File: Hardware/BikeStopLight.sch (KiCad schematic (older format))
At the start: 60 parts, among them J1 ST-Link, J2 PWR, J3 BAT, J4 Conn_01x01, J5 Conn_01x01, J6 Conn_01x08, Q1 NTD4909N, U1 MCP1703A-3302_SOT23, U2 STM32L052K8Tx, U3 RFM95W-868S2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

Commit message: WIP - Started layout
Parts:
- added C25, C27: 100 nF, Capacitor_SMD:C_0805_2012Metric, symbol Device:C_Small
- added C26: TBC, Capacitor_SMD:C_0805_2012Metric, symbol Device:C_Small
- C1, C10, C11, C12, C13, C14, C15, C16, C17, C18, C19, C20, C21, C22, C23, C24, C3, C4, C5, C6, C7, C8, C9: footprint Capacitor_SMD:C_0603_1608Metric_Pad1.05x0.95mm_HandSolder -> Capacitor_SMD:C_0805_2012Metric
- C2: footprint Capacitor_SMD:C_0805_2012Metric_Pad1.15x1.40mm_HandSolder -> Capacitor_SMD:C_0805_2012Metric
- J1: footprint (none) -> Connector_PinHeader_2.54mm:PinHeader_1x04_P2.54mm_Vertical
- J2: footprint (none) -> Connector_PinHeader_2.54mm:PinHeader_1x03_P2.54mm_Vertical
- J3: footprint (none) -> Connector_PinHeader_2.54mm:PinHeader_1x02_P2.54mm_Vertical
- J4, J5: footprint (none) -> Connector_PinHeader_2.54mm:PinHeader_1x01_P2.54mm_Vertical
- J6: footprint (none) -> Connector_PinHeader_2.54mm:PinHeader_1x08_P2.54mm_Vertical
- R1, R3, R4, R5, R7: footprint Resistor_SMD:R_0603_1608Metric_Pad1.05x0.95mm_HandSolder -> Resistor_SMD:R_0805_2012Metric
- R6: value 0 Ohm -> 10 kOhm; footprint Resistor_SMD:R_0603_1608Metric_Pad1.05x0.95mm_HandSolder -> Resistor_SMD:R_0805_2012Metric
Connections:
- net labels added: BNO_INT_EXTI5, I2C1_SCL, I2C1_SDA, PWR_ON, SX_ANT, SX_DIO0, SX_DIO1, TSC_G2_IO1_S, TSC_G2_IO2, TSC_G2_IO3
- net labels removed: -BATT, INT, LED_ON, SCL, SDA
- wire segments 150 -> 182
- no-connect marks 7 -> 11
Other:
- note removed: "USB_DM"
- note removed: "USB_DP"
- moved on the sheet: J5

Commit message: WIP - Routed
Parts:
- removed J3: BAT, Connector_PinHeader_2.54mm:PinHeader_1x02_P2.54mm_Vertical, symbol Connector_Generic:Conn_01x02
- added R8: 0 Ohm, Resistor_SMD:R_0805_2012Metric, symbol Device:R_Small
- added S2: Touch_IO2, symbol Connector_Generic:Conn_01x01
- added S3: Touch_IO3, symbol Connector_Generic:Conn_01x01
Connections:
- wire segments 182 -> 183
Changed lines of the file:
@@
 Wire Wire Line
 	1100 2250 1350 2250
-$Comp
-L Connector_Generic:Conn_01x02 J3
-U 1 1 5CD40FA1
-P 8550 2900
-F 0 "J3" H 8470 2575 50  0000 C CNN
-F 1 "BAT" H 8470 2666 50  0000 C CNN
-F 2 "Connector_PinHeader_2.54mm:PinHeader_1x02_P2.54mm_Vertical" H 8550 2900 50  0001 C CNN
-F 3 "~" H 8550 2900 50  0001 C CNN
-	1    8550 2900
-	-1   0    0    1
-$EndComp
-Wire Wire Line
-	8750 2900 9450 2900
-Wire Wire Line
-	9450 2800 8750 2800
-$Comp
-L power:+BATT #PWR0108
-U 1 1 5CD4BED2
-P 9450 2800
-F 0 "#PWR0108" H 9450 2650 50  0001 C CNN
-F 1 "+BATT" H 9465 2973 50  0000 C CNN
-F 2 "" H 9450 2800 50  0001 C CNN
-F 3 "" H 9450 2800 50  0001 C CNN
-	1    9450 2800
-	1    0    0    -1
-$EndComp
 Wire Wire Line
 	950  7400 1050 7400
@@
 	1    0    0    -1
 $EndComp
-Entry Wire Line
-	3950 6150 4050 6250
 Wire Wire Line
 	7050 3500 7150 3500
@@
 F 3 "http://www.hoperf.com/upload/rf/RFM95_96_97_98W.pdf" H 3300 6900 50  0001 C CNN
 	1    6600 5250
-	1    0    0    -1
-$EndComp
-$Comp
-L power:VCC #PWR0118
-U 1 1 5CD44CB6
-P 6600 4400
-F 0 "#PWR0118" H 6600 4250 50  0001 C CNN
-F 1 "VCC" H 6617 4573 50  0000 C CNN
-F 2 "" H 6600 4400 50  0001 C CNN
-F 3 "" H 6600 4400 50  0001 C CNN
-	1    6600 4400
 	1    0    0    -1
 $EndComp
@@
 	5500 1850 6050 1850
 Wire Wire Line
-	6050 1950 5500 1950
-Wire Wire Line
 	5500 2350 6050 2350
 Wire Wire Line
@@
 	2700 1900 2700 1850
 $Comp
-L power:GND #PWR0107
-U 1 1 5CE8B7EE
-P 9450 2900
-F 0 "#PWR0107" H 9450 2650 50  0001 C CNN
-F 1 "GND" H 9455 2727 50  0000 C CNN
-F 2 "" H 9450 2900 50  0001 C CNN
-F 3 "" H 9450 2900 50  0001 C CNN
-	1    9450 2900
-	1    0    0    -1
-$EndComp
+L power:+3.3V #PWR0118
+U 1 1 5CE124DA
+P 6600 4400
+F 0 "#PWR0118" H 6600 4250 50  0001 C CNN
+F 1 "+3.3V" H 6615 4573 50  0000 C CNN
+F 2 "" H 6600 4400 50  0001 C CNN
+F 3 "" H 6600 4400 50  0001 C CNN
+	1    6600 4400
+	1    0    0    -1
+$EndComp
+$Comp
+L Device:R_Small R8
+U 1 1 5CE13172
+P 750 1550
+F 0 "R8" H 809 1596 50  0000 L CNN
+F 1 "0 Ohm" H 809 1505 50  0000 L CNN
+F 2 "Resistor_SMD:R_0805_2012Metric" H 750 1550 50  0001 C CNN
+F 3 "~" H 750 1550 50  0001 C CNN
+	1    750  1550
+	1    0    0    -1
+$EndComp
+Wire Wire Line
+	750  1450 750  1100
+Connection ~ 750  1100
+Wire Wire Line
+	750  1650 750  1950
+Wire Wire Line
+	750  1950 850  1950
+Connection ~ 850  1950
+$Comp
+L Connector_Generic:Conn_01x01 S2
+U 1 1 5CE3D1CA
+P 6250 1850
+F 0 "S2" H 6330 1892 50  0000 L CNN
+F 1 "Touch_IO2" H 6330 1801 50  0000 L CNN
+F 2 "" H 6250 1850 50  0001 C CNN
+F 3 "~" H 6250 1850 50  0001 C CNN
+	1    6250 1850
+	1    0    0    -1
+$EndComp
+$Comp
+L Connector_Generic:Conn_01x01 S3
+U 1 1 5CE3D3C0
+P 6100 1950
+F 0 "S3" H 6180 1992 50  0000 L CNN
+F 1 "Touch_IO3" H 6180 1901 50  0000 L CNN
+F 2 "" H 6100 1950 50  0001 C CNN
+F 3 "~" H 6100 1950 50  0001 C CNN
+	1    6100 1950
+	1    0    0    -1
+$EndComp
+Wire Wire Line
+	5500 1950 5900 1950
 $EndSCHEMATC

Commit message: WIP - Add touch & GND via
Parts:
- S2, S3: footprint (none) -> Perso:Capacitive_Touch_6_mm
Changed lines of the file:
@@
 F 0 "S2" H 6330 1892 50  0000 L CNN
 F 1 "Touch_IO2" H 6330 1801 50  0000 L CNN
-F 2 "" H 6250 1850 50  0001 C CNN
+F 2 "Perso:Capacitive_Touch_6_mm" H 6250 1850 50  0001 C CNN
 F 3 "~" H 6250 1850 50  0001 C CNN
 	1    6250 1850
@@
 F 0 "S3" H 6180 1992 50  0000 L CNN
 F 1 "Touch_IO3" H 6180 1901 50  0000 L CNN
-F 2 "" H 6100 1950 50  0001 C CNN
+F 2 "Perso:Capacitive_Touch_6_mm" H 6100 1950 50  0001 C CNN
 F 3 "~" H 6100 1950 50  0001 C CNN
 	1    6100 1950

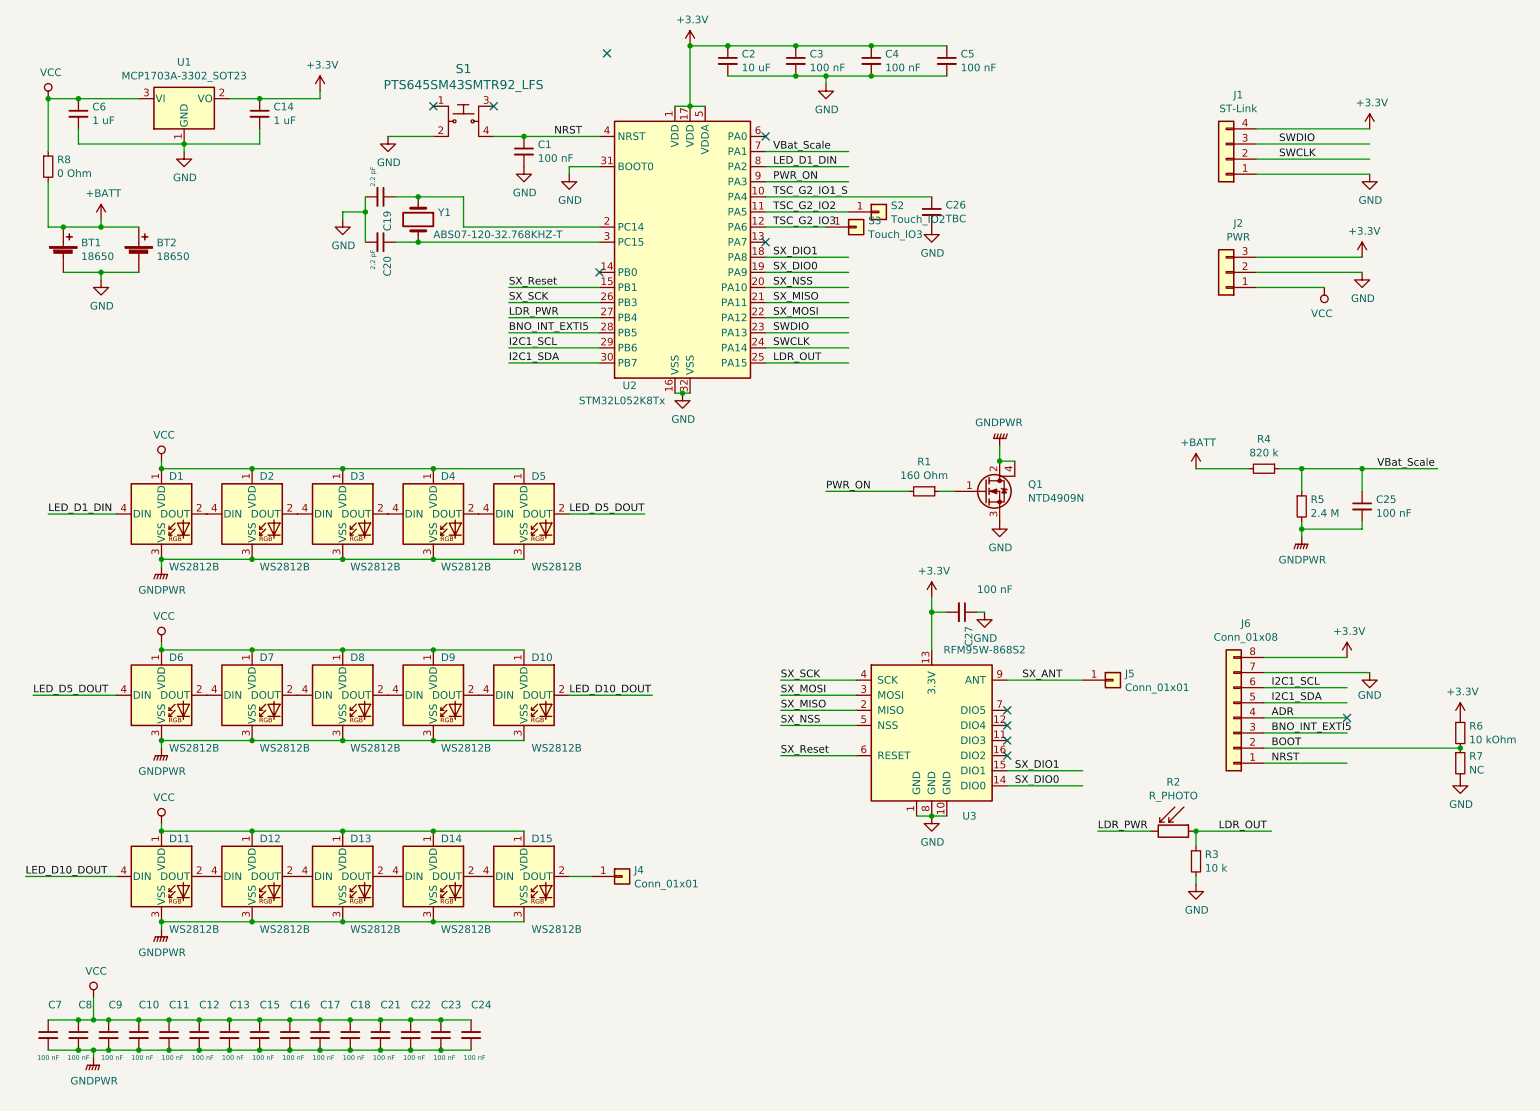
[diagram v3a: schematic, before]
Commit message: WIP - Add red light
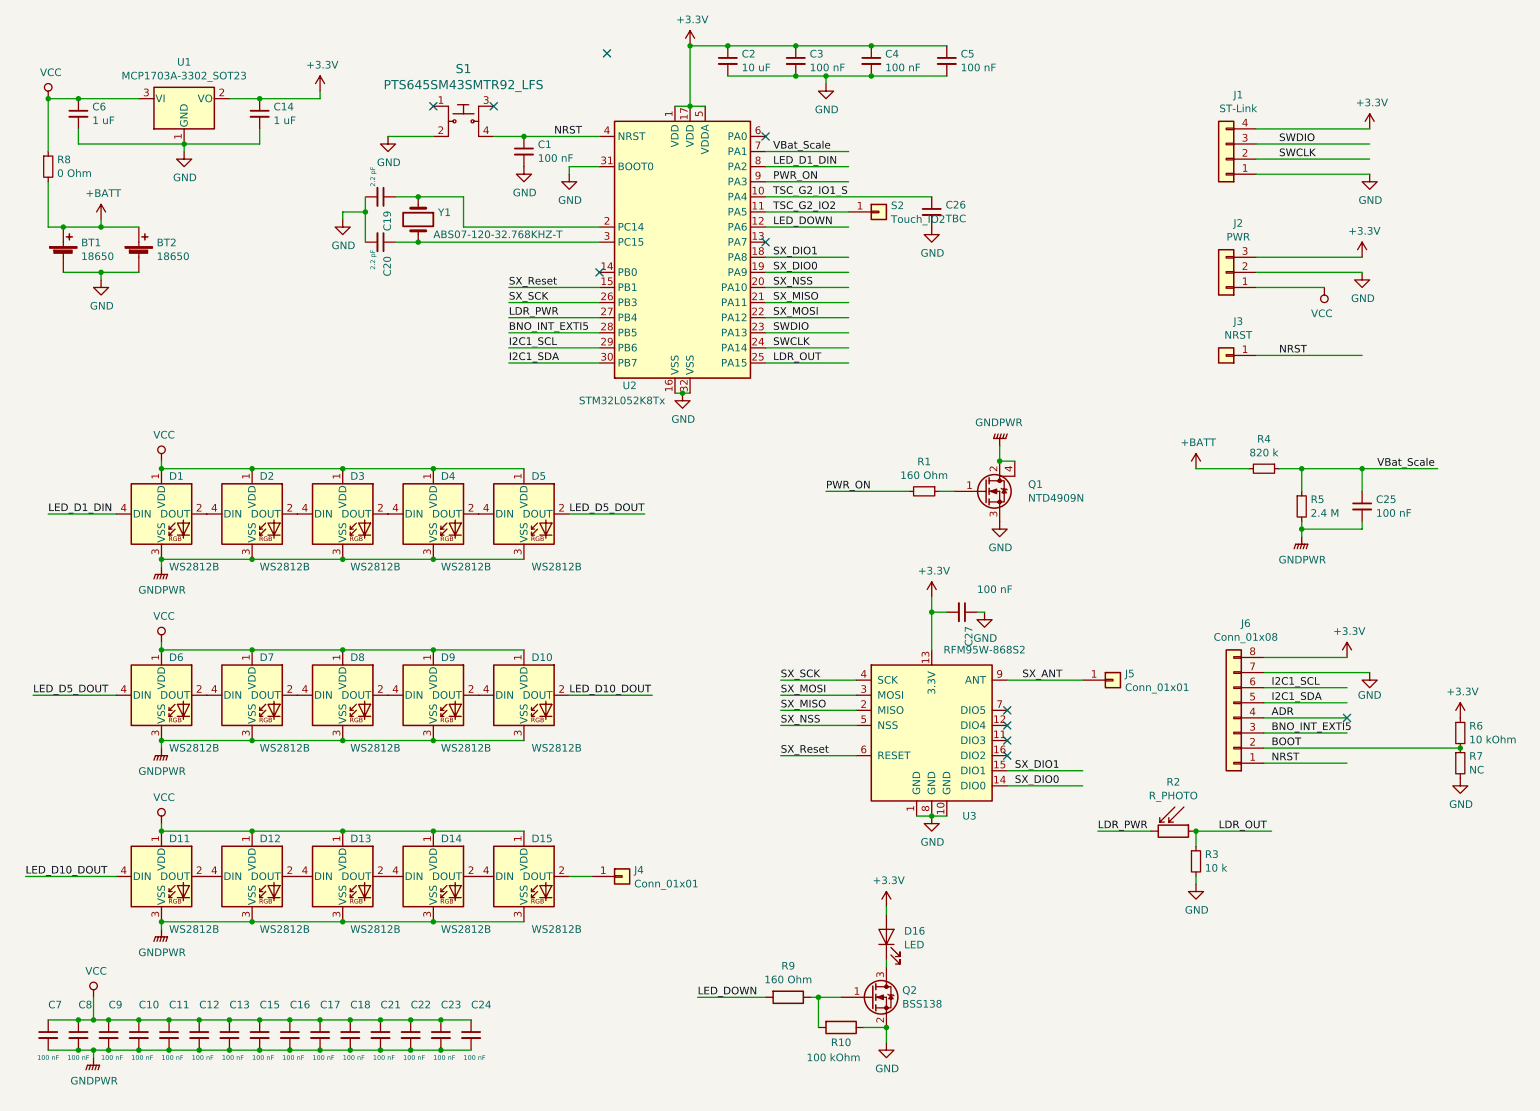
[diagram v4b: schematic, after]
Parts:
- removed S3: Touch_IO3, Perso:Capacitive_Touch_6_mm, symbol Connector_Generic:Conn_01x01
- added D16: LED, LED_THT:LED_D5.0mm, symbol Device:LED
- added J3: NRST, Connector_PinHeader_2.54mm:PinHeader_1x01_P2.54mm_Vertical, symbol Connector_Generic:Conn_01x01
- added Q2: BSS138, Package_TO_SOT_SMD:SOT-23, symbol Transistor_FET:BSS138
- added R10: 100 kOhm, Resistor_SMD:R_0805_2012Metric, symbol Device:R
- added R9: 160 Ohm, Resistor_SMD:R_0805_2012Metric, symbol Device:R
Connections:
- net labels added: LED_DOWN
- net labels removed: TSC_G2_IO3
- wire segments 183 -> 192
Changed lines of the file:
@@
 TSC_G2_IO2
 Text Label 5550 1950 0    50   ~ 0
-TSC_G2_IO3
+LED_DOWN
 Text Label 5550 1750 0    50   ~ 0
 TSC_G2_IO1_S
@@
 $EndComp
 $Comp
-L Connector_Generic:Conn_01x01 S3
-U 1 1 5CE3D3C0
-P 6100 1950
-F 0 "S3" H 6180 1992 50  0000 L CNN
-F 1 "Touch_IO3" H 6180 1901 50  0000 L CNN
-F 2 "Perso:Capacitive_Touch_6_mm" H 6100 1950 50  0001 C CNN
-F 3 "~" H 6100 1950 50  0001 C CNN
-	1    6100 1950
-	1    0    0    -1
-$EndComp
-Wire Wire Line
-	5500 1950 5900 1950
+L Transistor_FET:BSS138 Q2
+U 1 1 5D00C2FB
+P 6200 7050
+F 0 "Q2" H 6405 7096 50  0000 L CNN
+F 1 "BSS138" H 6405 7005 50  0000 L CNN
+F 2 "Package_TO_SOT_SMD:SOT-23" H 6400 6975 50  0001 L CIN
+F 3 "https://www.fairchildsemi.com/datasheets/BS/BSS138.pdf" H 6200 7050 50  0001 L CNN
+	1    6200 7050
+	1    0    0    -1
+$EndComp
+$Comp
+L Device:R R9
+U 1 1 5D00C4D4
+P 5650 7050
+F 0 "R9" V 5443 7050 50  0000 C CNN
+F 1 "160 Ohm" V 5534 7050 50  0000 C CNN
+F 2 "Resistor_SMD:R_0805_2012Metric" V 5580 7050 50  0001 C CNN
+F 3 "~" H 5650 7050 50  0001 C CNN
+	1    5650 7050
+	0    1    1    0
+$EndComp
+$Comp
+L Device:R R10
+U 1 1 5D00C61D
+P 6000 7250
+F 0 "R10" V 6100 7250 50  0000 C CNN
+F 1 "100 kOhm" V 6200 7200 50  0000 C CNN
+F 2 "Resistor_SMD:R_0805_2012Metric" V 5930 7250 50  0001 C CNN
+F 3 "~" H 6000 7250 50  0001 C CNN
+	1    6000 7250
+	0    1    1    0
+$EndComp
+$Comp
+L power:+3.3V #PWR0107
+U 1 1 5D00C972
+P 6300 6450
+F 0 "#PWR0107" H 6300 6300 50  0001 C CNN
+F 1 "+3.3V" H 6315 6623 50  0000 C CNN
+F 2 "" H 6300 6450 50  0001 C CNN
+F 3 "" H 6300 6450 50  0001 C CNN
+	1    6300 6450
+	1    0    0    -1
+$EndComp
+$Comp
+L Device:LED D16
+U 1 1 5D00CCC5
+P 6300 6650
+F 0 "D16" V 6338 6533 50  0000 R CNN
+F 1 "LED" V 6247 6533 50  0000 R CNN
+F 2 "LED_THT:LED_D5.0mm" H 6300 6650 50  0001 C CNN
+F 3 "~" H 6300 6650 50  0001 C CNN
+	1    6300 6650
+	0    -1   -1   0
+$EndComp
+Wire Wire Line
+	6150 7250 6300 7250
+Connection ~ 6300 7250
+Wire Wire Line
+	5800 7050 5850 7050
+Wire Wire Line
+	5850 7250 5850 7050
+Connection ~ 5850 7050
+Wire Wire Line
+	5850 7050 6000 7050
+Wire Wire Line
+	6300 6450 6300 6500
+Wire Wire Line
+	6300 6800 6300 6850
+Wire Wire Line
+	6300 7250 6300 7350
+$Comp
+L power:GND #PWR0108
+U 1 1 5D073B78
+P 6300 7350
+F 0 "#PWR0108" H 6300 7100 50  0001 C CNN
+F 1 "GND" H 6305 7177 50  0000 C CNN
+F 2 "" H 6300 7350 50  0001 C CNN
+F 3 "" H 6300 7350 50  0001 C CNN
+	1    6300 7350
+	1    0    0    -1
+$EndComp
+Wire Wire Line
+	5500 1950 6050 1950
+Text Label 5050 7050 0    50   ~ 0
+LED_DOWN
+Wire Wire Line
+	5050 7050 5500 7050
+$Comp
+L Connector_Generic:Conn_01x01 J3
+U 1 1 5D04E11D
+P 8550 2800
+F 0 "J3" H 8470 2575 50  0000 C CNN
+F 1 "NRST" H 8470 2666 50  0000 C CNN
+F 2 "Connector_PinHeader_2.54mm:PinHeader_1x01_P2.54mm_Vertical" H 8550 2800 50  0001 C CNN
+F 3 "~" H 8550 2800 50  0001 C CNN
+	1    8550 2800
+	-1   0    0    1
+$EndComp
+Wire Wire Line
+	8750 2800 9450 2800
+Text Label 8900 2800 0    50   ~ 0
+NRST
 $EndSCHEMATC

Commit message: Add reset connector
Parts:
- added R11: 165 Ohm, Resistor_SMD:R_0805_2012Metric, symbol Device:R_Small
- S1: symbol dk_Tactile-Switches:PTS645SM43SMTR92_LFS -> BikeStopLight-rescue:PTS645SM43SMTR92_LFS-dk_Tactile-Switches
- U3: symbol RF_AM_FM:RFM95W-868S2 -> BikeStopLight-rescue:RFM95W-868S2-RF_AM_FM
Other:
- moved on the sheet: D16, Q2, R10, R9
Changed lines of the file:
@@
 EESchema Schematic File Version 4
 LIBS:BikeStopLight-cache
-EELAYER 26 0
+EELAYER 29 0
 EELAYER END
 $Descr A4 11693 8268
@@
 VBat_Scale
 $Comp
-L RF_AM_FM:RFM95W-868S2 U3
+L BikeStopLight-rescue:RFM95W-868S2-RF_AM_FM U3
 U 1 1 5CD3D42D
 P 6600 5250
@@
 $EndComp
 $Comp
-L dk_Tactile-Switches:PTS645SM43SMTR92_LFS S1
+L BikeStopLight-rescue:PTS645SM43SMTR92_LFS-dk_Tactile-Switches S1
 U 1 1 5CE533E2
 P 3500 1250
@@
 L Transistor_FET:BSS138 Q2
 U 1 1 5D00C2FB
-P 6200 7050
-F 0 "Q2" H 6405 7096 50  0000 L CNN
-F 1 "BSS138" H 6405 7005 50  0000 L CNN
-F 2 "Package_TO_SOT_SMD:SOT-23" H 6400 6975 50  0001 L CIN
-F 3 "https://www.fairchildsemi.com/datasheets/BS/BSS138.pdf" H 6200 7050 50  0001 L CNN
-	1    6200 7050
+P 6200 7200
+F 0 "Q2" H 6405 7246 50  0000 L CNN
+F 1 "BSS138" H 6405 7155 50  0000 L CNN
+F 2 "Package_TO_SOT_SMD:SOT-23" H 6400 7125 50  0001 L CIN
+F 3 "https://www.fairchildsemi.com/datasheets/BS/BSS138.pdf" H 6200 7200 50  0001 L CNN
+	1    6200 7200
 	1    0    0    -1
 $EndComp
@@
 L Device:R R9
 U 1 1 5D00C4D4
-P 5650 7050
-F 0 "R9" V 5443 7050 50  0000 C CNN
-F 1 "160 Ohm" V 5534 7050 50  0000 C CNN
-F 2 "Resistor_SMD:R_0805_2012Metric" V 5580 7050 50  0001 C CNN
-F 3 "~" H 5650 7050 50  0001 C CNN
-	1    5650 7050
+P 5650 7200
+F 0 "R9" V 5443 7200 50  0000 C CNN
+F 1 "160 Ohm" V 5534 7200 50  0000 C CNN
+F 2 "Resistor_SMD:R_0805_2012Metric" V 5580 7200 50  0001 C CNN
+F 3 "~" H 5650 7200 50  0001 C CNN
+	1    5650 7200
 	0    1    1    0
 $EndComp
@@
 L Device:R R10
 U 1 1 5D00C61D
-P 6000 7250
-F 0 "R10" V 6100 7250 50  0000 C CNN
-F 1 "100 kOhm" V 6200 7200 50  0000 C CNN
-F 2 "Resistor_SMD:R_0805_2012Metric" V 5930 7250 50  0001 C CNN
-F 3 "~" H 6000 7250 50  0001 C CNN
-	1    6000 7250
+P 6000 7400
+F 0 "R10" V 6100 7400 50  0000 C CNN
+F 1 "100 kOhm" V 6200 7350 50  0000 C CNN
+F 2 "Resistor_SMD:R_0805_2012Metric" V 5930 7400 50  0001 C CNN
+F 3 "~" H 6000 7400 50  0001 C CNN
+	1    6000 7400
 	0    1    1    0
 $EndComp
@@
 L power:+3.3V #PWR0107
 U 1 1 5D00C972
-P 6300 6450
-F 0 "#PWR0107" H 6300 6300 50  0001 C CNN
-F 1 "+3.3V" H 6315 6623 50  0000 C CNN
-F 2 "" H 6300 6450 50  0001 C CNN
-F 3 "" H 6300 6450 50  0001 C CNN
-	1    6300 6450
+P 6300 6400
+F 0 "#PWR0107" H 6300 6250 50  0001 C CNN
+F 1 "+3.3V" H 6315 6573 50  0000 C CNN
+F 2 "" H 6300 6400 50  0001 C CNN
+F 3 "" H 6300 6400 50  0001 C CNN
+	1    6300 6400
 	1    0    0    -1
 $EndComp
@@
 L Device:LED D16
 U 1 1 5D00CCC5
-P 6300 6650
-F 0 "D16" V 6338 6533 50  0000 R CNN
-F 1 "LED" V 6247 6533 50  0000 R CNN
-F 2 "LED_THT:LED_D5.0mm" H 6300 6650 50  0001 C CNN
-F 3 "~" H 6300 6650 50  0001 C CNN
-	1    6300 6650
+P 6300 6800
+F 0 "D16" V 6338 6683 50  0000 R CNN
+F 1 "LED" V 6247 6683 50  0000 R CNN
+F 2 "LED_THT:LED_D5.0mm" H 6300 6800 50  0001 C CNN
+F 3 "~" H 6300 6800 50  0001 C CNN
+	1    6300 6800
 	0    -1   -1   0
 $EndComp
 Wire Wire Line
-	6150 7250 6300 7250
-Connection ~ 6300 7250
-Wire Wire Line
-	5800 7050 5850 7050
-Wire Wire Line
-	5850 7250 5850 7050
-Connection ~ 5850 7050
-Wire Wire Line
-	5850 7050 6000 7050
-Wire Wire Line
-	6300 6450 6300 6500
-Wire Wire Line
-	6300 6800 6300 6850
-Wire Wire Line
-	6300 7250 6300 7350
+	6150 7400 6300 7400
+Connection ~ 6300 7400
+Wire Wire Line
+	5800 7200 5850 7200
+Wire Wire Line
+	5850 7400 5850 7200
+Connection ~ 5850 7200
+Wire Wire Line
+	5850 7200 6000 7200
+Wire Wire Line
+	6300 6400 6300 6450
+Wire Wire Line
+	6300 6950 6300 7000
+Wire Wire Line
+	6300 7400 6300 7500
 $Comp
 L power:GND #PWR0108
 U 1 1 5D073B78
-P 6300 7350
-F 0 "#PWR0108" H 6300 7100 50  0001 C CNN
-F 1 "GND" H 6305 7177 50  0000 C CNN
-F 2 "" H 6300 7350 50  0001 C CNN
-F 3 "" H 6300 7350 50  0001 C CNN
-	1    6300 7350
+P 6300 7500
+F 0 "#PWR0108" H 6300 7250 50  0001 C CNN
+F 1 "GND" H 6305 7327 50  0000 C CNN
+F 2 "" H 6300 7500 50  0001 C CNN
+F 3 "" H 6300 7500 50  0001 C CNN
+	1    6300 7500
 	1    0    0    -1
 $EndComp
 Wire Wire Line
 	5500 1950 6050 1950
-Text Label 5050 7050 0    50   ~ 0
+Text Label 5050 7200 0    50   ~ 0
 LED_DOWN
 Wire Wire Line
-	5050 7050 5500 7050
+	5050 7200 5500 7200
 $Comp
 L Connector_Generic:Conn_01x01 J3
@@
 Text Label 8900 2800 0    50   ~ 0
 NRST
+$Comp
+L Device:R_Small R11
+U 1 1 5D1B8833
+P 6300 6550
+F 0 "R11" H 6359 6596 50  0000 L CNN
+F 1 "165 Ohm" H 6359 6505 50  0000 L CNN
+F 2 "Resistor_SMD:R_0805_2012Metric" H 6300 6550 50  0001 C CNN
+F 3 "~" H 6300 6550 50  0001 C CNN
+	1    6300 6550
+	1    0    0    -1
+$EndComp
 $EndSCHEMATC
